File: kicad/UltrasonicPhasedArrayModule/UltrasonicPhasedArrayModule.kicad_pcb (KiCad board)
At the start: 2 copper layers, 65 x 62 mm, 12 parts, among them J1 Conn_02x08_Top_Bottom, Q1 2N2222, Q2 2N2222, Q3 2N2222, Q4 2N2222, U1 74HC138, U2 74HC04

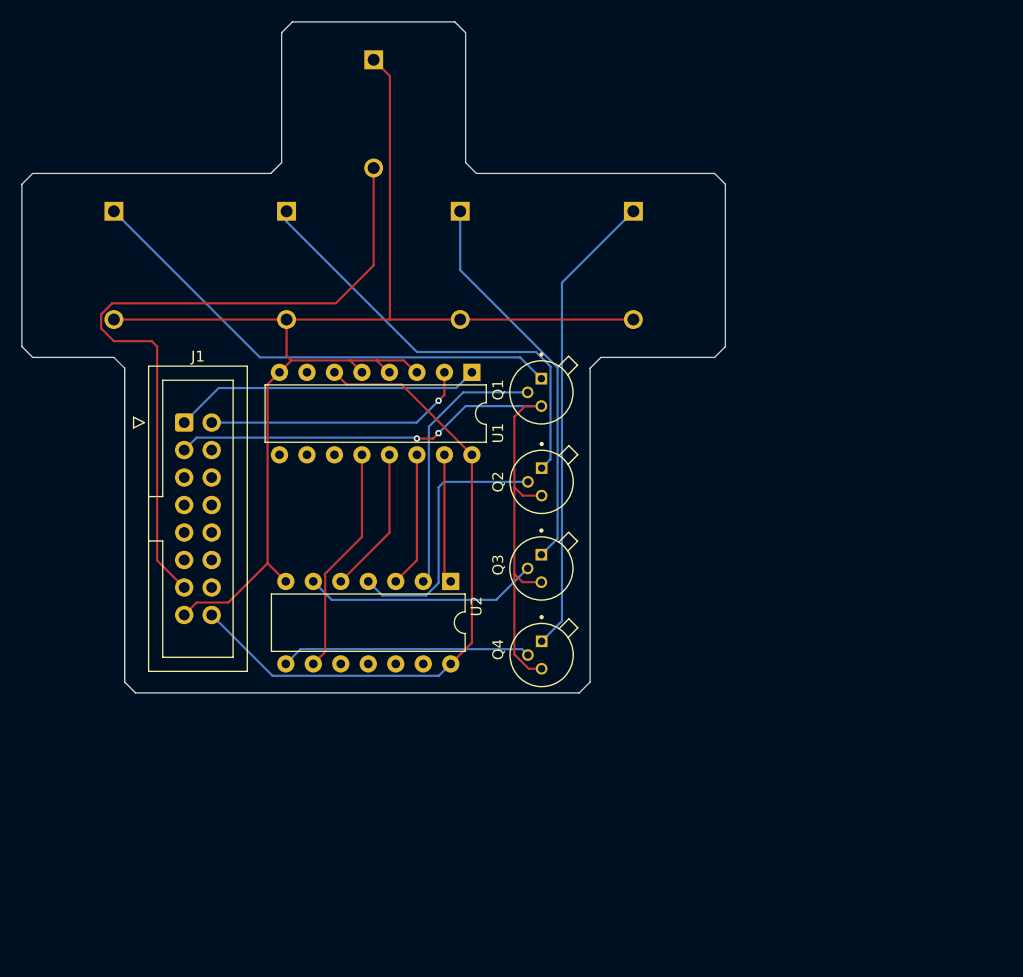
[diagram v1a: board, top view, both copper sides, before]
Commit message: KiCAD Files Completed and General UPA Update
KiCAD design files for the base module and UPA module are completed and on order.

The UPA sensor code is now fully operational. One issue: accuracy of the beam forming. A recalculation of delay timing is required. EEPROM does not seem to write/read properly on breadboard, though this could be to faulty connections. Further testing is required.

KNOWN ISSUES:
* UPA beam forming not accurate
* EEPROM fails to read/write properly.
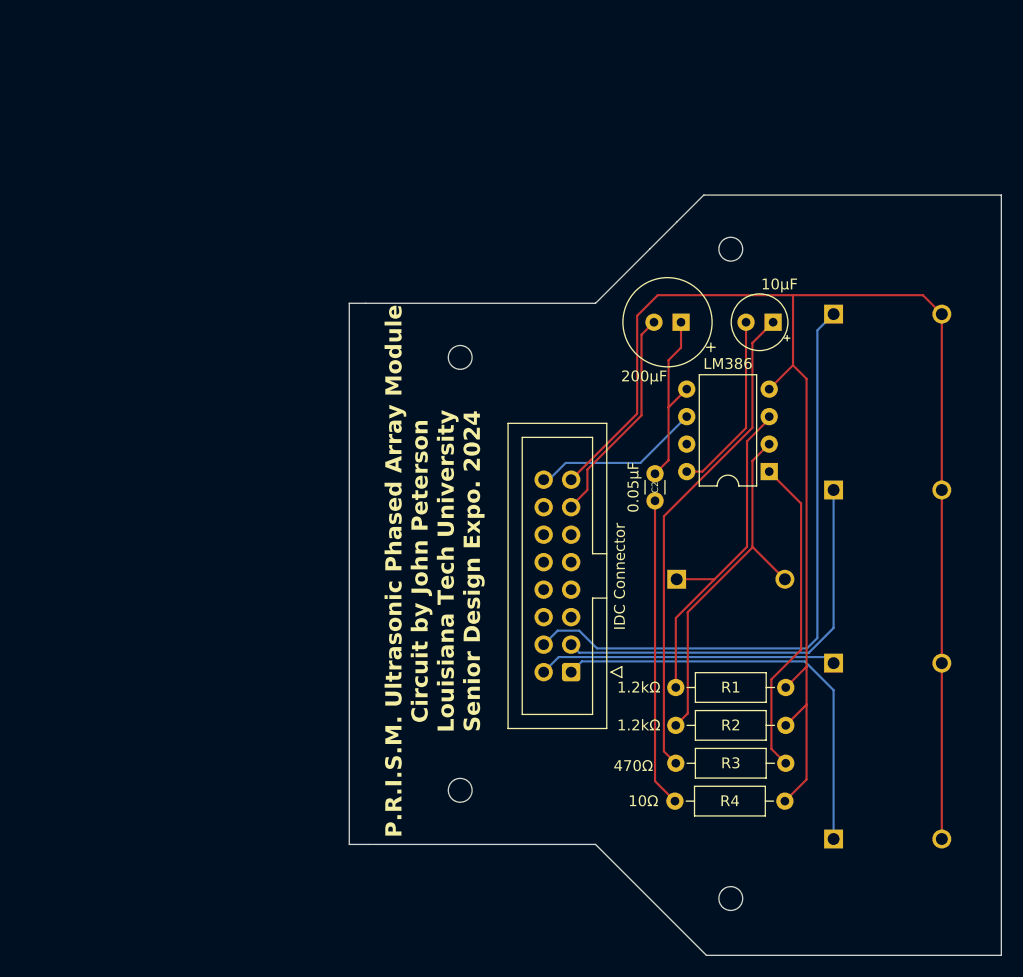
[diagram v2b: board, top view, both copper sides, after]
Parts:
- removed MK1: Microphone_Ultrasound, UltrasonicTransducerReceiver:Ultrasonic Transducer-Receiver
- removed Q1, Q2, Q3, Q4: 2N2222, 2N2222:TO127P584H533-3
- removed U2: 74HC04, Package_DIP:DIP-14_W7.62mm
- added C1: 200μF, Capacitor_THT:CP_Radial_Tantal_D8.0mm_P2.50mm, F.Cu at (145.4, 51.8)
- added C2: 0.05μF, Capacitor_THT:C_Disc_D3.0mm_W1.6mm_P2.50mm, F.Cu at (143.0, 65.8)
- added C3: 10μF, Capacitor_THT:CP_Radial_Tantal_D5.0mm_P2.50mm, F.Cu at (153.9, 51.7)
- added R1: 1.2kΩ, Resistor_THT:R_Axial_DIN0207_L6.3mm_D2.5mm_P10.16mm_Horizontal, F.Cu at (144.9, 85.5)
- added R2: 1.2kΩ, Resistor_THT:R_Axial_DIN0207_L6.3mm_D2.5mm_P10.16mm_Horizontal, F.Cu at (155.1, 89.0)
- added R3: 470Ω, Resistor_THT:R_Axial_DIN0207_L6.3mm_D2.5mm_P10.16mm_Horizontal, F.Cu at (144.9, 92.5)
- added R4: 10Ω, Resistor_THT:R_Axial_DIN0207_L6.3mm_D2.5mm_P10.16mm_Horizontal, F.Cu at (155.0, 96.0)
- added REF**: MountingHole_2.2mm_M2, MountingHole:MountingHole_2.2mm_M2, F.Cu at (150.0, 45.0)
- added REF**: MountingHole_2.2mm_M2, MountingHole:MountingHole_2.2mm_M2, F.Cu at (125.0, 55.0)
- added REF**: MountingHole_2.2mm_M2, MountingHole:MountingHole_2.2mm_M2, F.Cu at (150.0, 105.0)
- added REF**: MountingHole_2.2mm_M2, MountingHole:MountingHole_2.2mm_M2, F.Cu at (125.0, 95.0)
- added Receiver 0: Microphone_Ultrasound, UltrasonicTransducerReceiver:Ultrasonic Transducer-Receiver, B.Cu at (145.0, 75.5)
- J1: value Conn_02x08_Top_Bottom -> IDC Connector
- LS1: value Speaker_Ultrasound -> Transducer 3
- LS2: value Speaker_Ultrasound -> Transducer 2
- LS3: value Speaker_Ultrasound -> Transducer 1
- LS4: value Speaker_Ultrasound -> Transducer 0
- U1: value 74HC138 -> LM386; footprint Package_DIP:DIP-16_W7.62mm -> Package_DIP:DIP-8_W7.62mm
- moved LS1 88.2 mm to (159.5, 99.5), turned to 0 degrees
- moved LS2 65.6 mm to (159.5, 83.2), turned to 0 degrees
- moved LS3 43.1 mm to (159.5, 67.2), turned to 0 degrees
- moved J1 42.5 mm to (135.2, 84.1), turned to 180 degrees
- moved U1 29.0 mm to (153.6, 65.5), turned to 180 degrees
- moved LS4 20.8 mm to (159.5, 51.0), turned to 0 degrees
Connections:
- J1 pad 15: Net-(J1-Pin_15) -> /GND
- J1 pad 16: Net-(J1-Pin_16) -> /Vsys
- J1 pad 4: unconnected-(J1-Pin_4-Pad4) -> Net-(J1-Pin_4)
- LS1 pad 1: Net-(LS1-Pad1) -> Net-(J1-Pin_1)
- LS1 pad 2: Net-(J1-Pin_15) -> /GND
- LS2 pad 1: Net-(LS2-Pad1) -> Net-(J1-Pin_2)
- LS2 pad 2: Net-(J1-Pin_15) -> /GND
- LS3 pad 1: Net-(LS3-Pad1) -> Net-(J1-Pin_3)
- LS3 pad 2: Net-(J1-Pin_15) -> /GND
- LS4 pad 1: Net-(LS4-Pad1) -> Net-(J1-Pin_4)
- LS4 pad 2: Net-(J1-Pin_15) -> /GND
- U1 pad 1: Net-(J1-Pin_1) -> Net-(R3-Pad2)
- U1 pad 2: Net-(J1-Pin_2) -> Net-(MK1-+)
- U1 pad 3: Net-(J1-Pin_15) -> Net-(MK1--)
- U1 pad 4: Net-(J1-Pin_15) -> /GND
- U1 pad 5: Net-(J1-Pin_15) -> Net-(C1-Pad1)
- U1 pad 6: Net-(J1-Pin_16) -> /Vsys
- U1 pad 8: Net-(J1-Pin_15) -> Net-(C3-Pad2)
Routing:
- net /GND: track 0.00 -> 152.5 mm
- net Net-(J1-Pin_15): track 123.5 -> 0.00 mm
- net Net-(J1-Pin_16): track 60.9 -> 0.00 mm
- net Net-(J1-Pin_4): track 0.00 -> 57.5 mm
- net Net-(J1-Pin_13): track 66.5 -> 20.3 mm
- net Net-(LS1-Pad1): track 45.9 -> 0.00 mm
- net Net-(C3-Pad1): track 0.00 -> 45.4 mm
- net Net-(LS4-Pad1): track 43.2 -> 0.00 mm
- net Net-(LS2-Pad1): track 40.6 -> 0.00 mm
- net Net-(LS3-Pad1): track 36.1 -> 0.00 mm
- net Net-(MK1-+): track 0.00 -> 33.8 mm
- net Net-(MK1--): track 0.00 -> 32.1 mm
- net Net-(J1-Pin_3): track 68.3 -> 38.3 mm, vias 2 -> 0
- net Net-(R3-Pad2): track 0.00 -> 29.9 mm
- net Net-(C2-Pad2): track 0.00 -> 28.5 mm
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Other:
- board size 65 x 62 mm -> 60.2 x 70.2 mm
- board text added: "P.R.I.S.M. Ultrasonic Phased Array Module Circuit by John Peterson Louisiana Tech University Senior Design Expo. 2024"
